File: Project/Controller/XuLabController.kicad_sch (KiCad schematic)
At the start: 4 parts, among them J1 Power

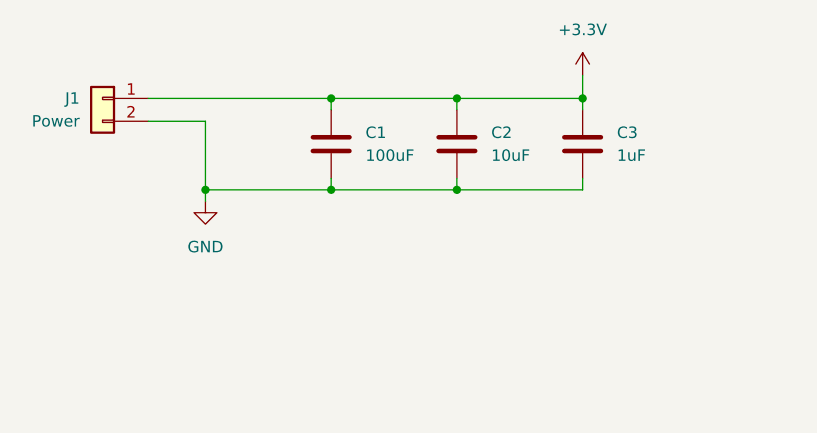
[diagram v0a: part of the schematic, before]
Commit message: Remove battery power from servo PWM connector
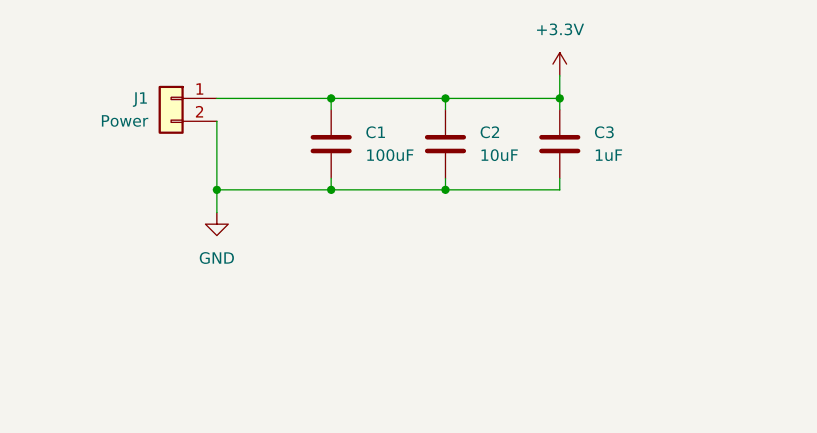
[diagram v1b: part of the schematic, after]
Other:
- moved on the sheet: C2, C3, J1
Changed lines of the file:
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@@
-	)
-	(junction
-		(at 78.74 25.4)
-		(diameter 0)
-		(color 0 0 0 0)
 	)
 	(junction
@@
 	)
 	(junction
-		(at 64.77 25.4)
+		(at 63.5 35.56)
 		(diameter 0)
 		(color 0 0 0 0)
 	)
 	(junction
-		(at 64.77 35.56)
+		(at 63.5 25.4)
 		(diameter 0)
 		(color 0 0 0 0)
 	)
 	(junction
-		(at 36.83 35.56)
+		(at 38.1 35.56)
 		(diameter 0)
 		(color 0 0 0 0)
@@
 	)
 	(junction
+		(at 76.2 25.4)
+		(diameter 0)
+		(color 0 0 0 0)
+	)
+	(junction
 		(at 256.54 29.21)
 		(diameter 0)
@@
 	(wire
 		(pts
-			(xy 64.77 35.56) (xy 64.77 34.29)
+			(xy 63.5 35.56) (xy 63.5 34.29)
 		)
 		(stroke
@@
 	(wire
 		(pts
+			(xy 38.1 35.56) (xy 50.8 35.56)
+		)
+		(stroke
+			(width 0)
+			(type default)
+		)
+	)
+	(wire
+		(pts
 			(xy 115.57 78.74) (xy 127 78.74)
 		)
@@
 	(wire
 		(pts
+			(xy 63.5 35.56) (xy 76.2 35.56)
+		)
+		(stroke
+			(width 0)
+			(type default)
+		)
+	)
+	(wire
+		(pts
 			(xy 165.1 105.41) (xy 176.53 105.41)
 		)
@@
 	(wire
 		(pts
-			(xy 78.74 26.67) (xy 78.74 25.4)
+			(xy 76.2 26.67) (xy 76.2 25.4)
 		)
 		(stroke
@@
 	(wire
 		(pts
-			(xy 78.74 35.56) (xy 78.74 34.29)
+			(xy 76.2 35.56) (xy 76.2 34.29)
 		)
 		(stroke
@@
 	(wire
 		(pts
-			(xy 36.83 27.94) (xy 30.48 27.94)
-		)
-		(stroke
-			(width 0)
-			(type default)
-		)
-	)
-	(wire
-		(pts
 			(xy 115.57 74.93) (xy 127 74.93)
 		)
@@
 	(wire
 		(pts
-			(xy 30.48 25.4) (xy 50.8 25.4)
+			(xy 38.1 25.4) (xy 50.8 25.4)
 		)
 		(stroke
@@
 	(wire
 		(pts
-			(xy 36.83 36.83) (xy 36.83 35.56)
+			(xy 38.1 38.1) (xy 38.1 35.56)
 		)
 		(stroke
@@
 	(wire
 		(pts
-			(xy 50.8 25.4) (xy 64.77 25.4)
+			(xy 50.8 25.4) (xy 63.5 25.4)
 		)
 		(stroke
@@
 	(wire
 		(pts
-			(xy 78.74 22.86) (xy 78.74 25.4)
+			(xy 76.2 22.86) (xy 76.2 25.4)
 		)
 		(stroke
@@
 	(wire
 		(pts
-			(xy 64.77 25.4) (xy 64.77 26.67)
+			(xy 63.5 25.4) (xy 63.5 26.67)
 		)
 		(stroke
@@
 	(wire
 		(pts
-			(xy 50.8 35.56) (xy 64.77 35.56)
-		)
-		(stroke
-			(width 0)
-			(type default)
-		)
-	)
-	(wire
-		(pts
-			(xy 36.83 35.56) (xy 50.8 35.56)
+			(xy 50.8 35.56) (xy 63.5 35.56)
 		)
 		(stroke
@@
 	(wire
 		(pts
-			(xy 64.77 35.56) (xy 78.74 35.56)
-		)
-		(stroke
-			(width 0)
-			(type default)
-		)
-	)
-	(wire
-		(pts
 			(xy 165.1 67.31) (xy 176.53 67.31)
 		)
@@
 	(wire
 		(pts
-			(xy 64.77 25.4) (xy 78.74 25.4)
-		)
-		(stroke
-			(width 0)
-			(type default)
-		)
-	)
-	(wire
-		(pts
 			(xy 165.1 129.54) (xy 172.72 129.54)
 		)
@@
 	(wire
 		(pts
+			(xy 63.5 25.4) (xy 76.2 25.4)
+		)
+		(stroke
+			(width 0)
+			(type default)
+		)
+	)
+	(wire
+		(pts
 			(xy 165.1 133.35) (xy 172.72 133.35)
 		)
@@
 	(wire
 		(pts
-			(xy 36.83 27.94) (xy 36.83 35.56)
+			(xy 38.1 27.94) (xy 38.1 35.56)
 		)
 		(stroke
@@
 	(symbol
 		(lib_id "power:GND")
-		(at 36.83 36.83 0)
+		(at 38.1 38.1 0)
 		(unit 1)
 		(exclude_from_sim no)
@@
 		(fields_autoplaced yes)
 		(property "Reference" "#PWR02"
-			(at 36.83 43.18 0)
+			(at 38.1 44.45 0)
 			(effects
 				(font
@@
 		)
 		(property "Value" "GND"
-			(at 36.83 41.91 0)
+			(at 38.1 43.18 0)
 			(effects
 				(font
@@
 		)
 		(property "Footprint" ""
-			(at 36.83 36.83 0)
+			(at 38.1 38.1 0)
 			(effects
 				(font
@@
 		)
 		(property "Datasheet" ""
-			(at 36.83 36.83 0)
+			(at 38.1 38.1 0)
 			(effects
 				(font
@@
 		)
 		(property "Description" "Power symbol creates a global label with name \"GND\" , ground"
-			(at 36.83 36.83 0)
+			(at 38.1 38.1 0)
 			(effects
 				(font
@@
 	(symbol
 		(lib_id "Device:C")
-		(at 78.74 30.48 0)
+		(at 76.2 30.48 0)
 		(unit 1)
 		(exclude_from_sim no)
@@
 		(fields_autoplaced yes)
 		(property "Reference" "C3"
-			(at 82.55 29.2099 0)
+			(at 80.01 29.2099 0)
 			(effects
 				(font
@@
 		)
 		(property "Value" "1uF"
-			(at 82.55 31.7499 0)
+			(at 80.01 31.7499 0)
 			(effects
 				(font
@@
 		)
 		(property "Footprint" "Capacitor_SMD:C_0603_1608Metric"
-			(at 79.7052 34.29 0)
+			(at 77.1652 34.29 0)
 			(effects
 				(font
@@
 		)
 		(property "Datasheet" "https://weblib.samsungsem.com/mlcc/mlcc-ec-data-sheet.do?partNumber=CL10B105KO8NNN"
-			(at 78.74 30.48 0)
+			(at 76.2 30.48 0)
 			(effects
 				(font
@@
 		)
 		(property "Description" "Unpolarized capacitor"
-			(at 78.74 30.48 0)
+			(at 76.2 30.48 0)
 			(effects
 				(font
@@
 		)
 		(property "Listing" "https://www.digikey.com/en/products/detail/samsung-electro-mechanics/CL10B105KO8NNNC/3886677"
-			(at 78.74 30.48 0)
+			(at 76.2 30.48 0)
 			(effects
 				(font
@@
 		)
 		(property "Interchangeable" "Yes"
-			(at 78.74 30.48 0)
+			(at 76.2 30.48 0)
 			(effects
 				(font
@@
 	(symbol
 		(lib_id "power:+3.3V")
-		(at 78.74 22.86 0)
+		(at 76.2 22.86 0)
 		(unit 1)
 		(exclude_from_sim no)
@@
 		(fields_autoplaced yes)
 		(property "Reference" "#PWR01"
-			(at 78.74 26.67 0)
+			(at 76.2 26.67 0)
 			(effects
 				(font
@@
 		)
 		(property "Value" "+3.3V"
-			(at 78.74 17.78 0)
+			(at 76.2 17.78 0)
 			(effects
 				(font
@@
 		)
 		(property "Footprint" ""
-			(at 78.74 22.86 0)
+			(at 76.2 22.86 0)
 			(effects
 				(font
@@
 		)
 		(property "Datasheet" ""
-			(at 78.74 22.86 0)
+			(at 76.2 22.86 0)
 			(effects
 				(font
@@
 		)
 		(property "Description" "Power symbol creates a global label with name \"+3.3V\""
-			(at 78.74 22.86 0)
+			(at 76.2 22.86 0)
 			(effects
 				(font
@@
 	(symbol
 		(lib_id "Connector_Generic:Conn_01x02")
-		(at 25.4 25.4 0)
+		(at 33.02 25.4 0)
 		(mirror y)
 		(unit 1)
@@
 		(dnp no)
 		(property "Reference" "J1"
-			(at 22.86 25.3999 0)
+			(at 30.48 25.3999 0)
 			(effects
 				(font
@@
 		)
 		(property "Value" "Power"
-			(at 22.86 27.9399 0)
+			(at 30.48 27.9399 0)
 			(effects
 				(font
@@
 		)
 		(property "Footprint" "Connector_JST:JST_XH_S2B-XH-A_1x02_P2.50mm_Horizontal"
-			(at 25.4 25.4 0)
+			(at 33.02 25.4 0)
 			(effects
 				(font
@@
 		)
 		(property "Datasheet" "https://www.jst-mfg.com/product/pdf/eng/eXH.pdf"
-			(at 25.4 25.4 0)
+			(at 33.02 25.4 0)
 			(effects
 				(font
@@
 		)
 		(property "Description" "Generic connector, single row, 01x02, script generated (kicad-library-utils/schlib/autogen/connector/)"
-			(at 25.4 25.4 0)
+			(at 33.02 25.4 0)
 			(effects
 				(font
@@
 		)
 		(property "Listing" "https://www.digikey.com/en/products/detail/jst-sales-america-inc/S2B-XH-A/1651055"
-			(at 25.4 25.4 0)
+			(at 33.02 25.4 0)
 			(effects
 				(font
@@
 		)
 		(property "Interchangeable" "No"
-			(at 25.4 25.4 0)
+			(at 33.02 25.4 0)
 			(effects
 				(font
@@
 	(symbol
 		(lib_id "Device:C")
-		(at 64.77 30.48 0)
+		(at 63.5 30.48 0)
 		(unit 1)
 		(exclude_from_sim no)
@@
 		(fields_autoplaced yes)
 		(property "Reference" "C2"
-			(at 68.58 29.2099 0)
+			(at 67.31 29.2099 0)
 			(effects
 				(font
@@
 		)
 		(property "Value" "10uF"
-			(at 68.58 31.7499 0)
+			(at 67.31 31.7499 0)
 			(effects
 				(font
@@
 		)
 		(property "Footprint" "Capacitor_SMD:C_1206_3216Metric"
-			(at 65.7352 34.29 0)
+			(at 64.4652 34.29 0)
 			(effects
 				(font
@@
 		)
 		(property "Datasheet" "https://mm.digikey.com/Volume0/opasdata/d220001/medias/docus/658/CL31B106KAHNNNE_Spec.pdf"
-			(at 64.77 30.48 0)
+			(at 63.5 30.48 0)
 			(effects
 				(font
@@
 		)
 		(property "Description" "Unpolarized capacitor"
-			(at 64.77 30.48 0)
+			(at 63.5 30.48 0)
 			(effects
 				(font
@@
 		)
 		(property "Listing" "https://www.digikey.com/en/products/detail/samsung-electro-mechanics/CL31B106KAHNNNE/3887462"
-			(at 64.77 30.48 0)
+			(at 63.5 30.48 0)
 			(effects
 				(font
@@
 		)
 		(property "Interchangeable" "Yes"
-			(at 64.77 30.48 0)
-			(effects
-				(font
+			(at 63.5 30.48 0)
+			(effects
+				(font

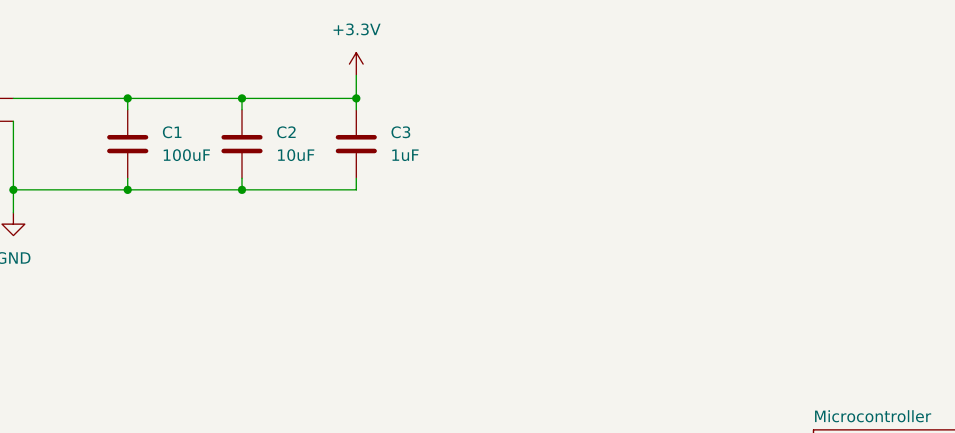
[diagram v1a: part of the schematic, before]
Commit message: Add LDO to power input for controller board
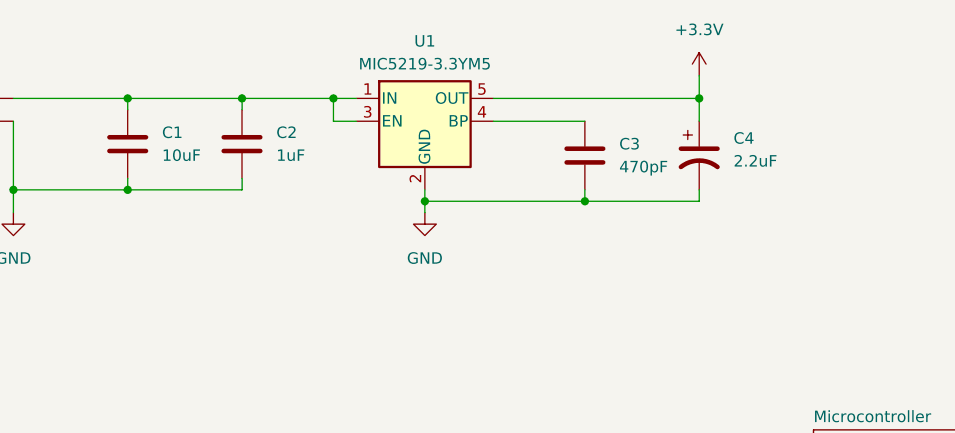
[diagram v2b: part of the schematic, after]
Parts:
- removed C1: 100uF, Capacitor_SMD:C_1210_3225Metric, symbol Device:C
- added C3: 470pF, Capacitor_SMD:C_0603_1608Metric, symbol Device:C
- added C4: 2.2uF, Capacitor_Tantalum_SMD:CP_EIA-3216-18_Kemet-A, symbol Device:C_Polarized_US
- added U1: MIC5219-3.3YM5, Package_TO_SOT_SMD:SOT-23-5, symbol Regulator_Linear:MIC5219-3.3YM5
- renumbered C2 to C1, C3 to C2
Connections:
- net +3.3V: now also C4.1, U1.5 (OUT); no longer C1.1, C2.1, J1.1 (Pin_1)
- net GND: now also C3.2, C4.2, U1.2 (GND)
- new net: C1.1, C2.1, J1.1 (Pin_1), U1.1 (IN), U1.3 (EN)
- new net: C3.1, U1.4 (BP)
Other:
- moved on the sheet: C1, C2

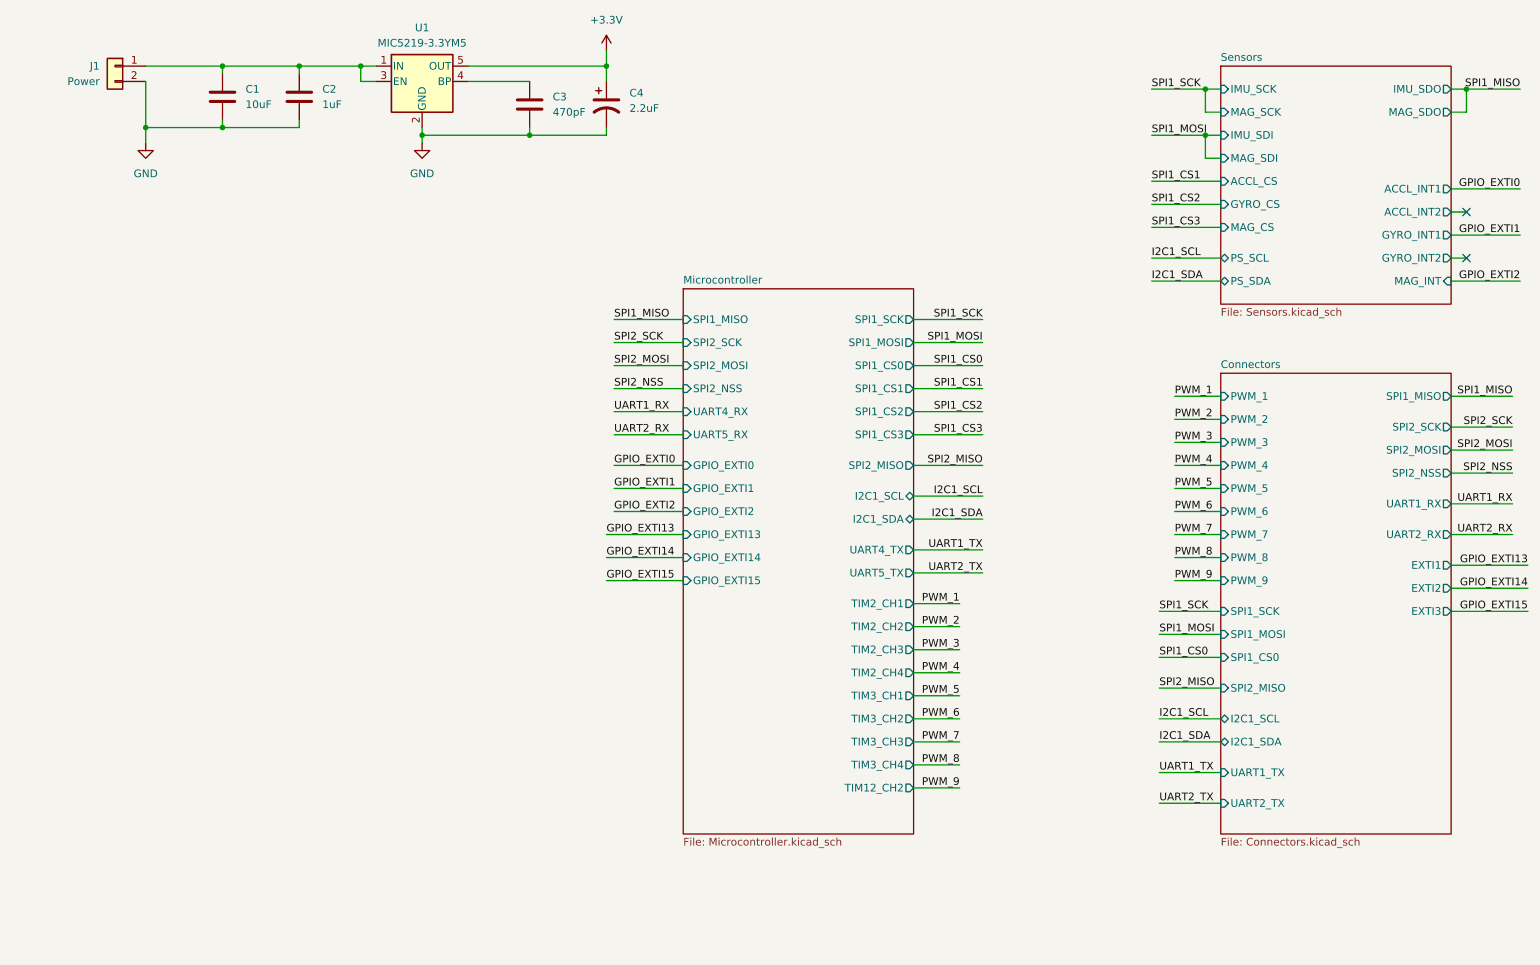
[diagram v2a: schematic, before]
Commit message: Add ideal diode ORing for power connector and USB power
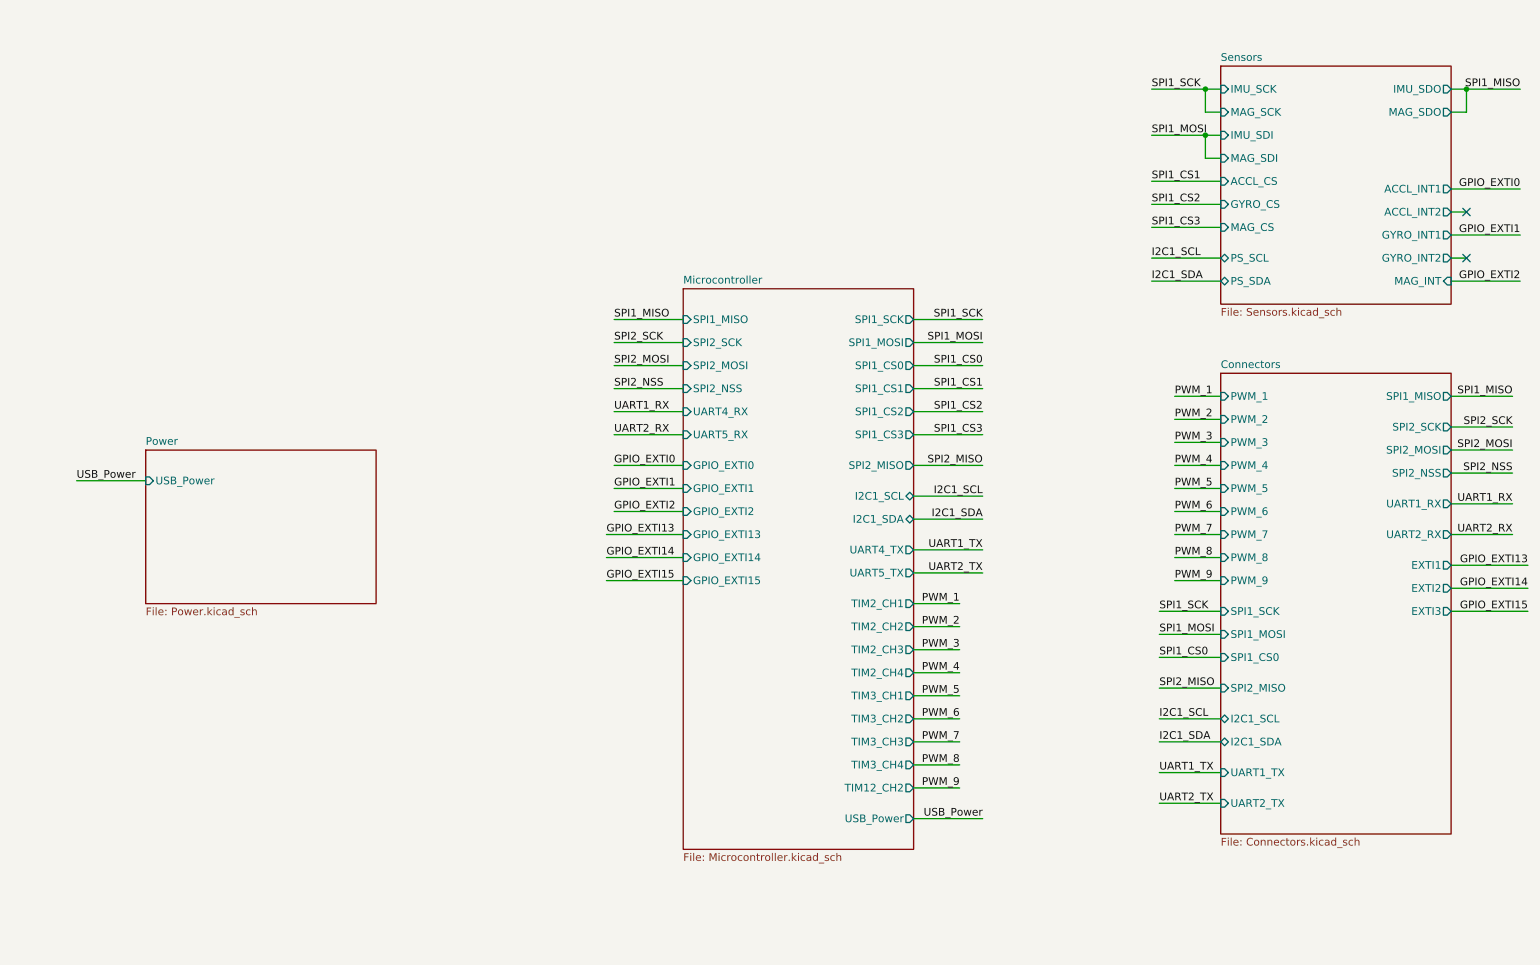
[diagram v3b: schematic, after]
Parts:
- removed C1: 10uF, Capacitor_SMD:C_1206_3216Metric, symbol Device:C
- removed C2: 1uF, Capacitor_SMD:C_0603_1608Metric, symbol Device:C
- removed C3: 470pF, Capacitor_SMD:C_0603_1608Metric, symbol Device:C
- removed C4: 2.2uF, Capacitor_Tantalum_SMD:CP_EIA-3216-18_Kemet-A, symbol Device:C_Polarized_US
- removed J1: Power, Connector_JST:JST_XH_S2B-XH-A_1x02_P2.50mm_Horizontal, symbol Connector_Generic:Conn_01x02
- removed U1: MIC5219-3.3YM5, Package_TO_SOT_SMD:SOT-23-5, symbol Regulator_Linear:MIC5219-3.3YM5
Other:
- added sheet Power (Power.kicad_sch)
- sheet Microcontroller ports: added USB_Power; removed none

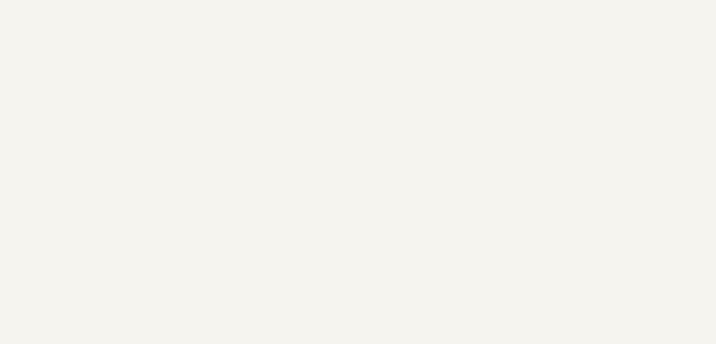
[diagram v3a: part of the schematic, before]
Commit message: Add 2.7mm M2.5 mounting holes
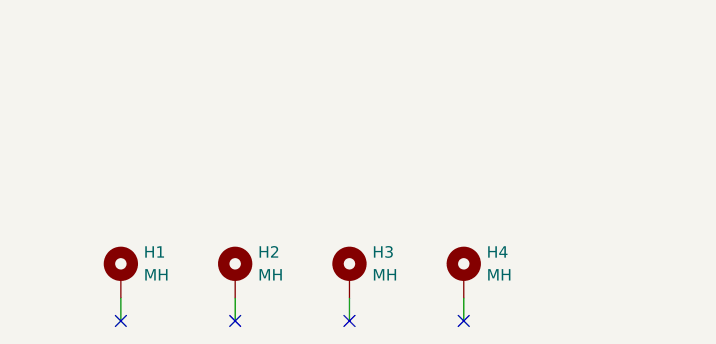
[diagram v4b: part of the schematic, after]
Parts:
- added H1, H2, H3, H4: MH, MountingHole:MountingHole_2.7mm_M2.5_Pad_Via, symbol Mechanical:MountingHole_Pad
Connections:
- no-connect marks 2 -> 6
